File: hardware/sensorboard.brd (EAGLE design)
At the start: 56 x 71 mm, 37 parts, among them U1 LM1117MP-3.3, U2 LM324D

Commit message: added I2C pull up resistors
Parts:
- added R19, R2: 4k7, rcl:R0805
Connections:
- net +3V3: now also R19.2, R2.2
- net SCL: now also R19.1
- net SDA: now also R2.1
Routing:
- net SCL: track 54.6 -> 65.9 mm
- net +3V3: track 147.7 -> 157.2 mm
- net SDA: track 56.1 -> 63.5 mm
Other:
- board text added: "20140219"
- board text removed: "20130904"
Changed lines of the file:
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@@
 <text x="52.8" y="67.6" size="1.778" layer="1" font="vector" ratio="10" rot="SR270">hexabus sensorboard</text>
 <hole x="13.46" y="60.25" drill="3.2"/>
-<text x="49.9" y="49.4" size="1.4224" layer="1" font="vector" ratio="12" rot="SR270">20130904</text>
+<text x="49.9" y="49.4" size="1.4224" layer="1" font="vector" ratio="12" rot="SR270">20140219</text>
 </plain>
 <attributes>
@@
 <attribute name="VALUE" x="18.25" y="20.84" size="1.27" layer="27"/>
 </element>
+<element name="R2" library="rcl" package="R0805" value="4k7" x="36.85" y="14.3"/>
+<element name="R19" library="rcl" package="R0805" value="4k7" x="36.85" y="12.2"/>
 </elements>
 <signals>
@@
 <wire x1="38.8" y1="26.63" x2="36.28" y2="24.11" width="0.254" layer="1"/>
 <wire x1="36.28" y1="24.11" x2="36.18" y2="24.11" width="0.254" layer="1"/>
+<contactref element="R2" pad="2"/>
+<contactref element="R19" pad="2"/>
+<wire x1="37.8" y1="14.3" x2="37.8" y2="12.2" width="0.254" layer="1"/>
+<wire x1="37.8" y1="14.3" x2="38.7" y2="15.2" width="0.254" layer="1"/>
+<wire x1="38.7" y1="15.2" x2="38.7" y2="19" width="0.254" layer="1"/>
+<wire x1="38.7" y1="19" x2="37.7" y2="20" width="0.254" layer="1"/>
+<wire x1="37.7" y1="20" x2="36.83" y2="20" width="0.254" layer="1"/>
 </signal>
 <signal name="+5V">
@@
 <wire x1="25.1" y1="28.9" x2="21.295" y2="28.9" width="0.254" layer="16"/>
 <wire x1="21.295" y1="28.9" x2="20.475" y2="28.08" width="0.254" layer="16"/>
-<wire x1="29.12" y1="23.78" x2="29.12" y2="12.45" width="0.254" layer="1"/>
+<wire x1="29.12" y1="23.78" x2="29.12" y2="12.9" width="0.254" layer="1"/>
+<wire x1="29.12" y1="12.9" x2="29.12" y2="12.45" width="0.254" layer="1"/>
 <wire x1="29.12" y1="12.45" x2="26.52" y2="9.85" width="0.254" layer="1"/>
 <wire x1="20.475" y1="28.08" x2="18.52" y2="28.08" width="0.254" layer="1"/>
@@
 <wire x1="16" y1="30.6" x2="16" y2="45.03" width="0.254" layer="1"/>
 <wire x1="16" y1="45.03" x2="9.33" y2="51.7" width="0.254" layer="1"/>
+<contactref element="R2" pad="1"/>
+<wire x1="35.9" y1="14.3" x2="35.3" y2="13.7" width="0.254" layer="1"/>
+<wire x1="35.3" y1="13.7" x2="29.92" y2="13.7" width="0.254" layer="1"/>
+<wire x1="29.92" y1="13.7" x2="29.12" y2="12.9" width="0.254" layer="1"/>
 </signal>
 <signal name="SCL">
@@
 <wire x1="16.9" y1="31.9" x2="16.9" y2="46.67" width="0.254" layer="1"/>
 <wire x1="11.87" y1="51.7" x2="16.9" y2="46.67" width="0.254" layer="1"/>
+<contactref element="R19" pad="1"/>
+<wire x1="35.9" y1="12.2" x2="35" y2="12.2" width="0.254" layer="1"/>
+<wire x1="35" y1="12.2" x2="33.9" y2="11.1" width="0.254" layer="1"/>
+<wire x1="33.9" y1="11.1" x2="30.27" y2="11.1" width="0.254" layer="1"/>
+<wire x1="30.27" y1="11.1" x2="26.52" y2="7.35" width="0.254" layer="1"/>
 </signal>
 <signal name="DQ">

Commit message: optimized some routes
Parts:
- moved R19 1.10 mm to (36.9, 11.1)
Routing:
- net +3V3: track 157.2 -> 159.4 mm
- net DQ: track 74.4 -> 75.2 mm
- net PD4: track 26.9 -> 27.7 mm
- net N$2: track 18.9 -> 19.5 mm
- net GND: vias 9 -> 12

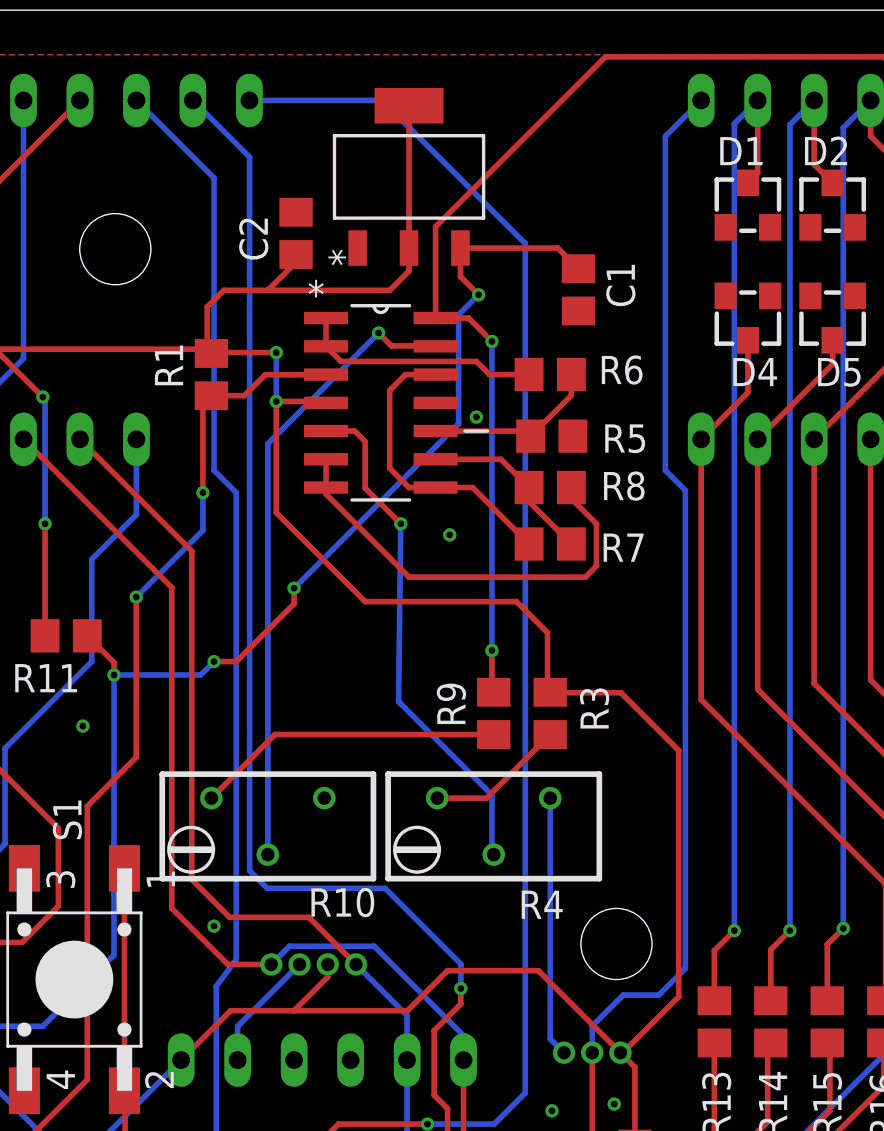
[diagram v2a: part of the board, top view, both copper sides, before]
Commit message: added a pinheader for calibrating the measure amplifier. fixes #2
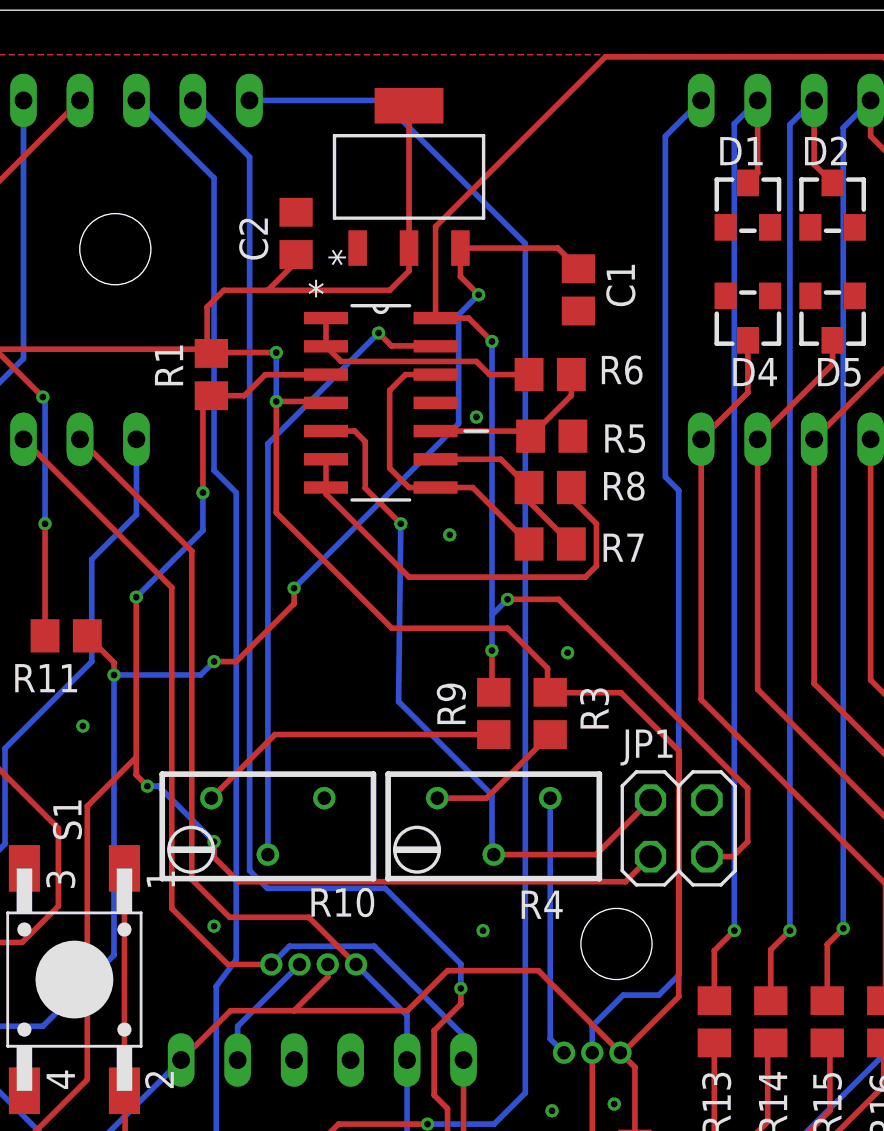
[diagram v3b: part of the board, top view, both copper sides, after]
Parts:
- added JP1: (no value), pinhead:2X02
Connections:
- net GND: now also JP1.4
- net OFFSET: now also JP1.2
- net PT100: now also JP1.1
- net TEMPERATURE: now also JP1.3
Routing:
- net PT100: track 58.7 -> 85.5 mm, vias 3 -> 5
- net TEMPERATURE: track 49.0 -> 68.8 mm, vias 2 -> 3
- net OFFSET: track 23.0 -> 31.0 mm
- net +3V3: track 159.4 -> 158.4 mm
- net GND: vias 12 -> 14
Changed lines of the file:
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@@
 <attribute name="NAME" x="38.815" y="10.37" size="1.27" layer="25"/>
 </element>
+<element name="JP1" library="pinhead" package="2X02" value="" x="38.8" y="34.2"/>
 </elements>
 <signals>
@@
 <via x="34.7" y="12.7" extent="1-16" drill="0.3"/>
 <via x="34.8" y="8.5" extent="1-16" drill="0.3"/>
+<contactref element="JP1" pad="4"/>
+<via x="30" y="29.6" extent="1-16" drill="0.3"/>
+<via x="33.8" y="42.1" extent="1-16" drill="0.3"/>
 </signal>
 <signal name="+3V3">
@@
 <wire x1="20.7" y1="53.4" x2="20.7" y2="55.6" width="0.254" layer="16"/>
 <wire x1="17.84" y1="55.5" x2="17.78" y2="55.56" width="0.254" layer="1"/>
-<wire x1="24.7" y1="44.4" x2="31.5" y2="44.4" width="0.254" layer="1"/>
-<wire x1="31.5" y1="44.4" x2="32.9" y2="43" width="0.254" layer="1"/>
-<wire x1="32.9" y1="43" x2="32.9" y2="40.44" width="0.254" layer="1"/>
 <wire x1="32.9" y1="40.44" x2="33.02" y2="40.32" width="0.254" layer="1"/>
 <wire x1="7.51" y1="16.81" x2="10.7" y2="20" width="0.254" layer="1"/>
@@
 <wire x1="20.7" y1="55.6" x2="17.82" y2="55.6" width="0.254" layer="1"/>
 <wire x1="17.82" y1="55.6" x2="17.78" y2="55.56" width="0.254" layer="1"/>
-<wire x1="20.7" y1="48.4" x2="24.7" y2="44.4" width="0.254" layer="1"/>
+<wire x1="20.7" y1="48.4" x2="25.9" y2="43.2" width="0.254" layer="1"/>
+<wire x1="25.9" y1="43.2" x2="31.1" y2="43.2" width="0.254" layer="1"/>
+<wire x1="32.9" y1="40.44" x2="32.9" y2="41.4" width="0.254" layer="1"/>
+<wire x1="32.9" y1="41.4" x2="31.1" y2="43.2" width="0.254" layer="1"/>
 </signal>
 <signal name="+5V">
@@
 <wire x1="20.2" y1="54.6" x2="19.26" y2="53.66" width="0.254" layer="1"/>
 <wire x1="19.26" y1="53.66" x2="17.78" y2="53.66" width="0.254" layer="1"/>
+<contactref element="JP1" pad="1"/>
+<wire x1="19" y1="31.8" x2="17.9" y2="32.9" width="0.254" layer="1"/>
+<wire x1="17.9" y1="32.9" x2="17.9" y2="33.6" width="0.254" layer="1"/>
+<via x="17.9" y="33.6" extent="1-16" drill="0.3"/>
+<wire x1="17.9" y1="33.6" x2="15.4" y2="36.1" width="0.254" layer="16"/>
+<wire x1="15.4" y1="36.1" x2="14.9" y2="36.1" width="0.254" layer="16"/>
+<via x="14.9" y="36.1" extent="1-16" drill="0.3"/>
+<wire x1="14.9" y1="36.1" x2="14.4" y2="36.6" width="0.254" layer="1"/>
+<wire x1="14.4" y1="36.6" x2="14.4" y2="37.4" width="0.254" layer="1"/>
+<wire x1="37.53" y1="32.93" x2="36.4" y2="31.8" width="0.254" layer="1"/>
+<wire x1="36.4" y1="31.8" x2="19" y2="31.8" width="0.254" layer="1"/>
 </signal>
 <signal name="OFFSET">
@@
 <wire x1="24.7" y1="51.6" x2="24.7" y2="49.5" width="0.254" layer="1"/>
 <wire x1="24.7" y1="49.5" x2="26.3" y2="47.9" width="0.254" layer="1"/>
+<contactref element="JP1" pad="2"/>
+<wire x1="30.48" y1="33.02" x2="35.08" y2="33.02" width="0.254" layer="1"/>
+<wire x1="35.08" y1="33.02" x2="37.53" y2="35.47" width="0.254" layer="1"/>
 </signal>
 <signal name="N$1">
@@
 <wire x1="48.01" y1="68.9" x2="49.97" y2="66.94" width="0.254" layer="1"/>
 <via x="30.4" y="42.2" extent="1-16" drill="0.3"/>
-<wire x1="30.4" y1="42.2" x2="30.4" y2="56.1" width="0.254" layer="16"/>
 <via x="30.4" y="56.1" extent="1-16" drill="0.3"/>
+<wire x1="30.4" y1="42.2" x2="30.4" y2="43.8" width="0.254" layer="16"/>
+<wire x1="30.4" y1="43.8" x2="30.4" y2="56.1" width="0.254" layer="16"/>
 <wire x1="27.8638" y1="57.15" x2="29.35" y2="57.15" width="0.254" layer="1"/>
 <wire x1="29.35" y1="57.15" x2="30.4" y2="56.1" width="0.254" layer="1"/>
 <wire x1="30.4" y1="42.2" x2="30.4" y2="40.4" width="0.254" layer="1"/>
 <wire x1="30.4" y1="40.4" x2="30.48" y2="40.32" width="0.254" layer="1"/>
+<contactref element="JP1" pad="3"/>
+<via x="31.1" y="44.5" extent="1-16" drill="0.3"/>
+<wire x1="41.9" y1="36" x2="41.9" y2="33.6" width="0.254" layer="1"/>
+<wire x1="41.9" y1="33.6" x2="41.23" y2="32.93" width="0.254" layer="1"/>
+<wire x1="41.23" y1="32.93" x2="40.07" y2="32.93" width="0.254" layer="1"/>
+<wire x1="31.1" y1="44.5" x2="30.4" y2="43.8" width="0.254" layer="16"/>
+<wire x1="31.1" y1="44.5" x2="33.4" y2="44.5" width="0.254" layer="1"/>
+<wire x1="33.4" y1="44.5" x2="41.9" y2="36" width="0.254" layer="1"/>
 </signal>
 <signal name="N$6">
@@
 <wire x1="34.91" y1="25.31" x2="36.3" y2="26.7" width="0.254" layer="16"/>
 <wire x1="36.3" y1="26.7" x2="37.9" y2="26.7" width="0.254" layer="16"/>
-<wire x1="37.9" y1="26.7" x2="39.1" y2="27.9" width="0.254" layer="16"/>
-<wire x1="39.1" y1="27.9" x2="39.1" y2="49.4" width="0.254" layer="16"/>
-<wire x1="39.1" y1="49.4" x2="38.2" y2="50.3" width="0.254" layer="16"/>
-<wire x1="38.2" y1="50.3" x2="38.2" y2="65.33" width="0.254" layer="16"/>
 <wire x1="38.2" y1="65.33" x2="39.81" y2="66.94" width="0.254" layer="16"/>
 <wire x1="26.52" y1="4.85" x2="28.95" y2="4.85" width="0.254" layer="1"/>
@@
 <wire x1="35.5" y1="18.1" x2="34.9" y2="18.7" width="0.254" layer="1"/>
 <wire x1="34.9" y1="18.7" x2="34.91" y2="18.71" width="0.254" layer="1"/>
+<wire x1="37.9" y1="26.7" x2="38.8" y2="27.6" width="0.254" layer="16"/>
+<wire x1="38.8" y1="27.6" x2="38.8" y2="49.4" width="0.254" layer="16"/>
+<wire x1="38.8" y1="49.4" x2="38.2" y2="50" width="0.254" layer="16"/>
+<wire x1="38.2" y1="50" x2="38.2" y2="65.33" width="0.254" layer="16"/>
 </signal>
 <signal name="GPIO1">

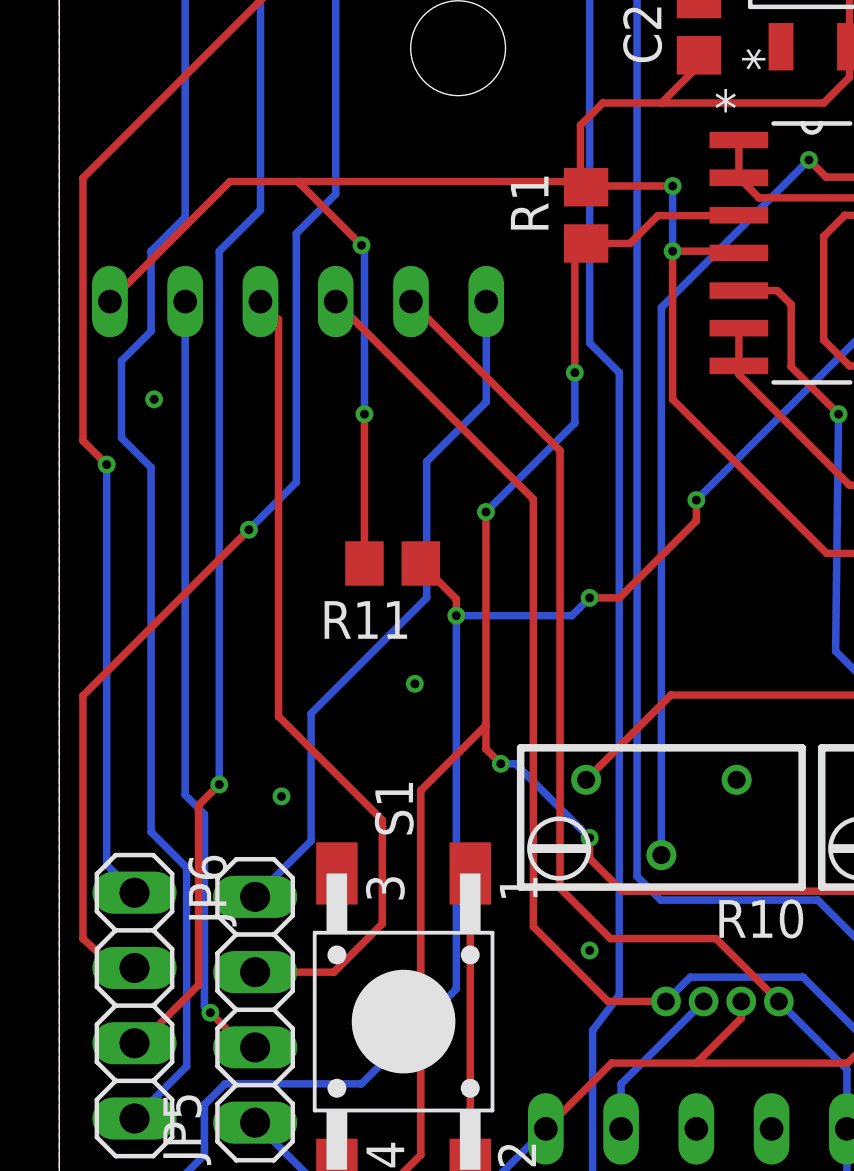
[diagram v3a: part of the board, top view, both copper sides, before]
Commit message: removed bypass resistor. see #5
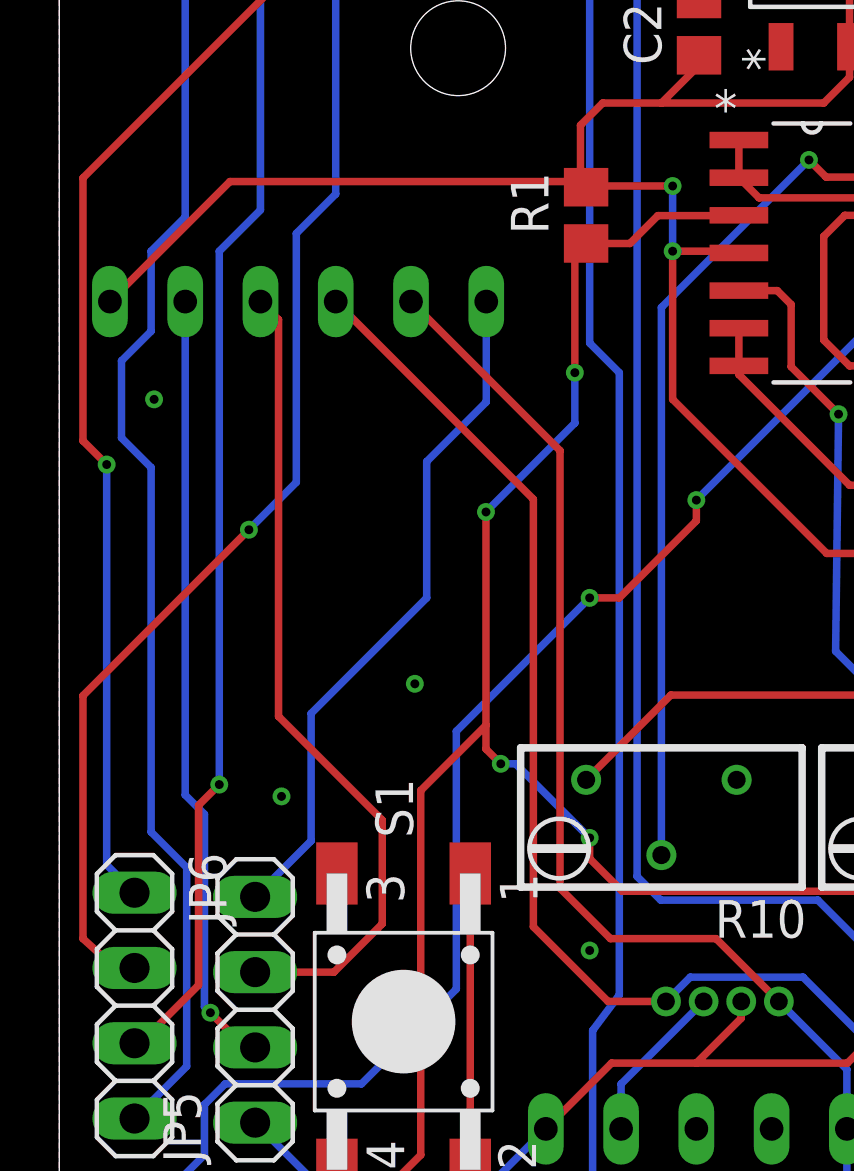
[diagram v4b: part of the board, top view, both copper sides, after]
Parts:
- removed R11: 0R, rcl:R0805
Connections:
- net +3V3: no longer R11.2
- net +5V: no longer R11.1
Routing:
- net +3V3: track 158.4 -> 144.6 mm, vias 5 -> 3
- net +5V: track 76.7 -> 72.1 mm, vias 4 -> 3
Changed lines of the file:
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@@
 <attribute name="NAME" x="35.185" y="54.18" size="1.27" layer="25"/>
-</element>
-<element name="R11" library="rcl" package="R0805" value="0R" x="11.25" y="42.86" smashed="yes" rot="R180">
-<attribute name="NAME" x="11.885" y="41.59" size="1.27" layer="25" rot="R180"/>
 </element>
 <element name="U2" library="hexasense" package="SOIC127P600X175-14N" value="LM324D" x="25.4" y="53.34" smashed="yes">
@@
 <contactref element="C2" pad="1"/>
 <contactref element="U1" pad="4"/>
-<contactref element="R11" pad="2"/>
 <contactref element="U2" pad="4"/>
 <contactref element="R1" pad="2"/>
@@
 <wire x1="20.7" y1="53.4" x2="22.8762" y2="53.4" width="0.254" layer="1"/>
 <wire x1="22.8762" y1="53.4" x2="22.9362" y2="53.34" width="0.254" layer="1"/>
-<wire x1="10.3" y1="42.86" x2="10.3" y2="47.9" width="0.254" layer="1"/>
-<via x="10.3" y="47.9" extent="1-16" drill="0.3"/>
-<wire x1="10.3" y1="47.9" x2="10.3" y2="53.5" width="0.254" layer="16"/>
-<wire x1="10.3" y1="53.5" x2="10.2" y2="53.6" width="0.254" layer="16"/>
-<via x="10.2" y="53.6" extent="1-16" drill="0.3"/>
 <wire x1="36.83" y1="20" x2="36.83" y2="23.46" width="0.254" layer="1"/>
 <wire x1="36.83" y1="23.46" x2="36.18" y2="24.11" width="0.254" layer="1"/>
@@
 <wire x1="33.02" y1="40.32" x2="33.02" y2="40.64" width="0.254" layer="1"/>
 <wire x1="20.7" y1="48.4" x2="20.7" y2="53.4" width="0.254" layer="1"/>
-<wire x1="17.59" y1="55.75" x2="8.1" y2="55.75" width="0.254" layer="1"/>
-<wire x1="8.1" y1="55.75" x2="5.76" y2="55.75" width="0.254" layer="1"/>
+<wire x1="17.59" y1="55.75" x2="5.76" y2="55.75" width="0.254" layer="1"/>
 <wire x1="5.76" y1="55.75" x2="1.71" y2="51.7" width="0.254" layer="1"/>
-<wire x1="10.2" y1="53.6" x2="8.1" y2="55.7" width="0.254" layer="1"/>
-<wire x1="8.1" y1="55.7" x2="8.1" y2="55.75" width="0.254" layer="1"/>
 <wire x1="17.59" y1="55.75" x2="17.59" y2="57.65" width="0.254" layer="1"/>
 <wire x1="17.59" y1="57.65" x2="18.34" y2="58.4" width="0.254" layer="1"/>
@@
 <contactref element="U1" pad="3"/>
 <contactref element="C1" pad="1"/>
-<contactref element="R11" pad="1"/>
 <contactref element="X1" pad="B3"/>
 <wire x1="34.29" y1="59.37" x2="33.3604" y2="60.2996" width="0.254" layer="1"/>
@@
 <via x="21.5" y="45" extent="1-16" drill="0.3"/>
 <via x="29.8" y="58.2" extent="1-16" drill="0.3"/>
-<via x="13.4" y="41.1" extent="1-16" drill="0.3"/>
 <wire x1="4.94" y1="11.81" x2="2.79" y2="11.81" width="0.254" layer="16"/>
 <wire x1="2.79" y1="11.81" x2="1.6" y2="13" width="0.254" layer="16"/>
@@
 <wire x1="29.8" y1="58.2" x2="28.9" y2="57.3" width="0.254" layer="16"/>
 <wire x1="28.9" y1="57.3" x2="28.9" y2="52.4" width="0.254" layer="16"/>
-<wire x1="13.4" y1="41.1" x2="13.4" y2="41.66" width="0.254" layer="1"/>
-<wire x1="13.4" y1="41.66" x2="12.2" y2="42.86" width="0.254" layer="1"/>
-<wire x1="13.4" y1="41.1" x2="17.3" y2="41.1" width="0.254" layer="16"/>
-<wire x1="17.3" y1="41.1" x2="17.9" y2="41.7" width="0.254" layer="16"/>
-<wire x1="13.4" y1="41.1" x2="13.4" y2="28.5" width="0.254" layer="16"/>
 <wire x1="21.5" y1="45" x2="21.5" y2="44.3" width="0.254" layer="1"/>
 <wire x1="21.5" y1="44.3" x2="18.9" y2="41.7" width="0.254" layer="1"/>
 <wire x1="21.5" y1="45" x2="28.9" y2="52.4" width="0.254" layer="16"/>
+<wire x1="13.4" y1="28.5" x2="13.4" y2="37.2" width="0.254" layer="16"/>
+<wire x1="13.4" y1="37.2" x2="17.9" y2="41.7" width="0.254" layer="16"/>
 </signal>
 <signal name="PT100">
